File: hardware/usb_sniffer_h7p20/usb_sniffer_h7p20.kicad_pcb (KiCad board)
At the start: 4 copper layers, 45 x 45 mm, 122 parts, among them J2 USB_C_Receptacle_USB2.0_16P, J3 USB_A, J4 USB_C_Receptacle_USB2.0_16P, J5 FFC-40P-0.5mm,NC, U1 H7P20N0L128-M3H1, U11 EA3036C, U2 LM2903, U3 LM2903, U4 LM2903, U5 USB3343, U6 P25Q32SH-SSH-IT, U7 CY7C68013A-56LTX, U8 24C64BN, X1 XO32,26M,NC, Y1 26M,NC, Y2 24M

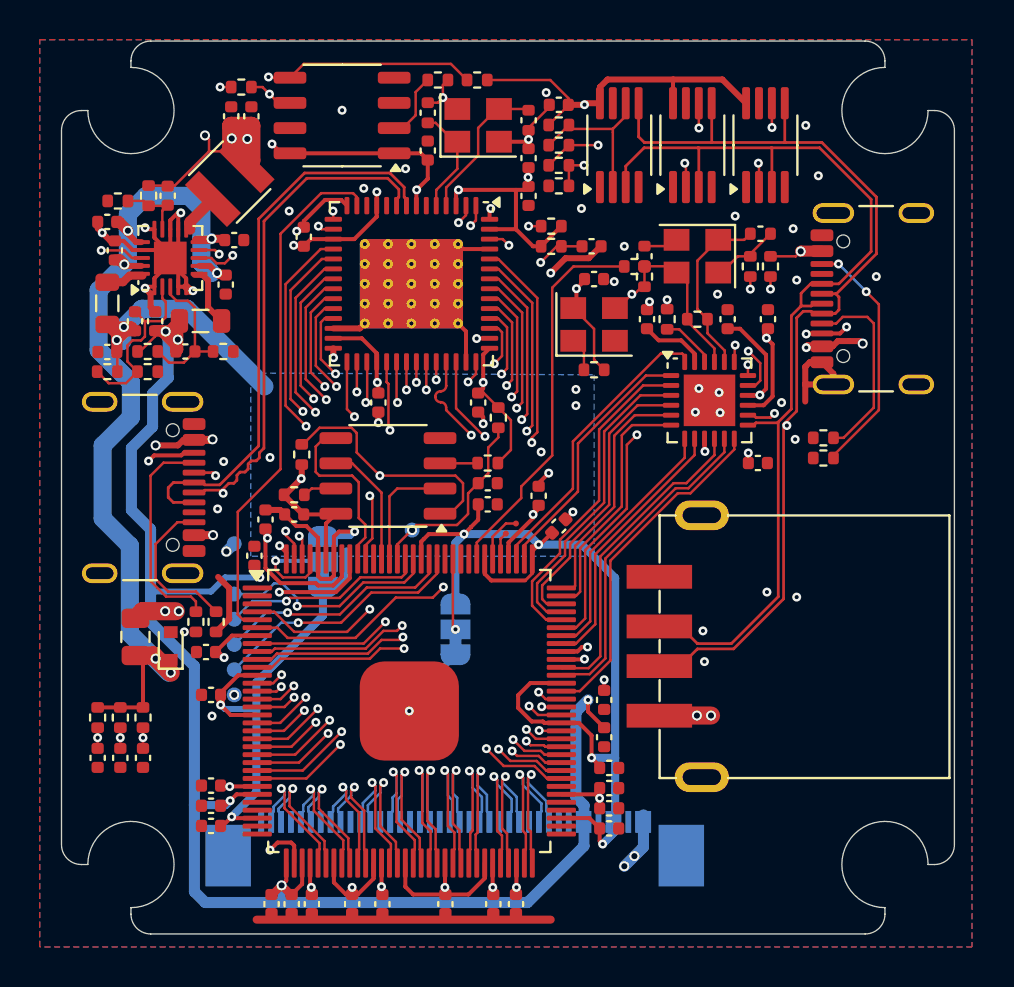
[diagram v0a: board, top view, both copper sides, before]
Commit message: 增加辅助电路和优化焊盘工艺
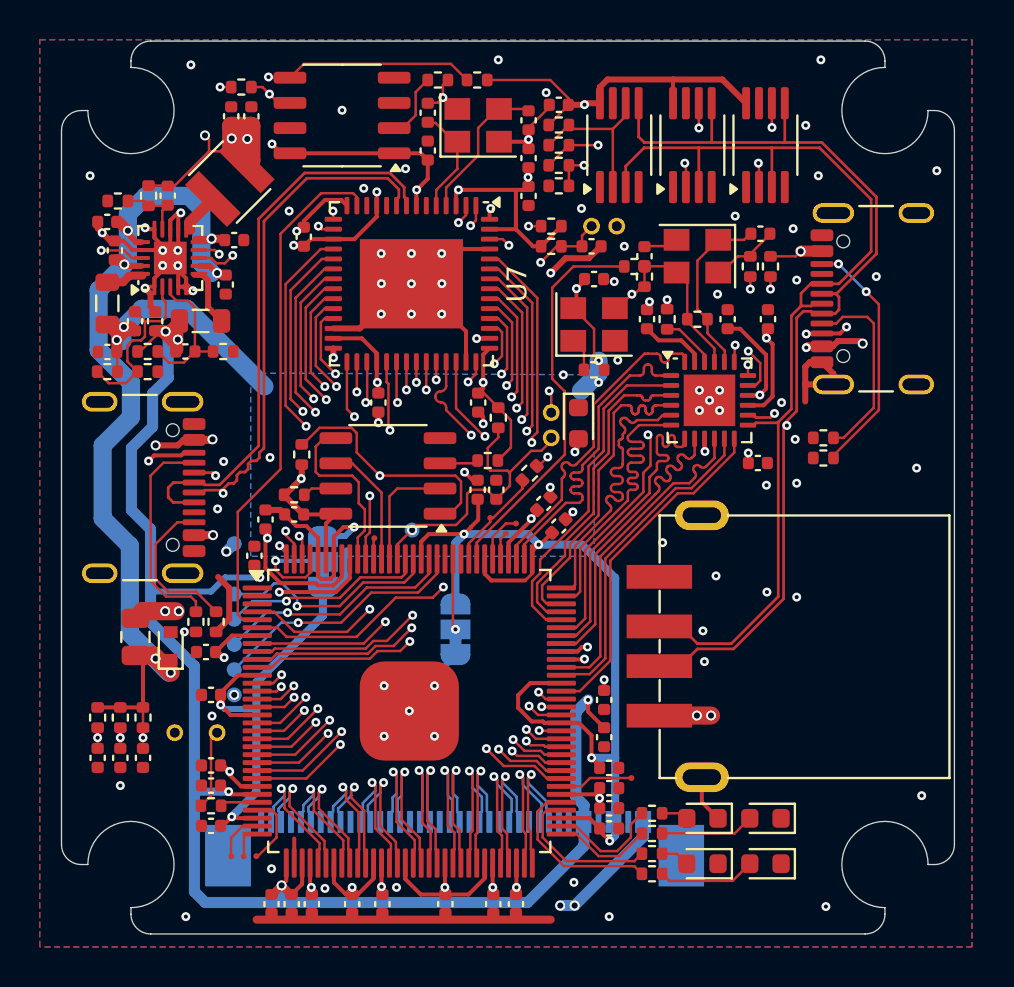
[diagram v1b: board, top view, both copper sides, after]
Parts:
- added D2: LED_RED, LED_SMD:LED_0603_1608Metric, F.Cu at (122.3, 114.2)
- added D3: LED_BLUE, LED_SMD:LED_0603_1608Metric, F.Cu at (125.5, 114.2)
- added D4: LED_YELLOW, LED_SMD:LED_0603_1608Metric, F.Cu at (122.3, 116.5)
- added D5: LED_GREEN, LED_SMD:LED_0603_1608Metric, F.Cu at (125.5, 116.5)
- added D6: LED_GREEN, LED_SMD:LED_0603_1608Metric, F.Cu at (116.1, 94.3)
- added R10: 4.7k, Resistor_SMD:R_0402_1005Metric, F.Cu at (119.8, 116.0)
- added R11: 5.1k, Resistor_SMD:R_0402_1005Metric, F.Cu at (119.8, 117.0)
- added R12: 5.1k, Resistor_SMD:R_0402_1005Metric, F.Cu at (113.6, 96.8)
- added R7: 470, Resistor_SMD:R_0402_1005Metric, F.Cu at (97.5, 113.5)
- added R8: 10k, Resistor_SMD:R_0402_1005Metric, F.Cu at (119.8, 113.9)
- added R9: 5.1k, Resistor_SMD:R_0402_1005Metric, F.Cu at (119.8, 114.9)
- added TP1: TestPoint, vllogic:PinHeader_1x01_P1.00mm_Vertical, F.Cu at (114.7, 95.0)
- added TP14: TestPoint, vllogic:PinHeader_1x01_P1.00mm_Vertical, F.Cu at (97.8, 109.9)
- added TP15: TestPoint, vllogic:PinHeader_1x01_P1.00mm_Vertical, F.Cu at (95.7, 109.9)
- added TP18: TestPoint, vllogic:TestPoint_Pad_D0.3mm, F.Cu at (111.6, 99.0)
- added TP19: TestPoint, vllogic:TestPoint_Pad_D0.3mm, F.Cu at (105.8, 100.1)
- added TP2: TestPoint, vllogic:PinHeader_1x01_P1.00mm_Vertical, F.Cu at (114.7, 93.7)
- added TP20: TestPoint, vllogic:TestPoint_Pad_D0.3mm, F.Cu at (99.8, 116.1)
- added TP21: TestPoint, vllogic:TestPoint_Pad_D0.3mm, F.Cu at (98.6, 116.1)
- added TP22: TestPoint, vllogic:TestPoint_Pad_D0.3mm, F.Cu at (99.2, 116.1)
- added TP23: TestPoint, vllogic:TestPoint_Pad_D0.3mm, F.Cu at (118.7, 112.1)
- added TP3: TestPoint, vllogic:PinHeader_1x01_P1.00mm_Vertical, F.Cu at (118.0, 84.3)
- added TP4: TestPoint, vllogic:PinHeader_1x01_P1.00mm_Vertical, F.Cu at (116.7, 84.3)
- C27: value 4.7uF -> 10uF
- C31, C32: value 20pF -> 12pF; footprint vllogic:C_0402_6mil -> Capacitor_SMD:C_0402_1005Metric
- C38: value 1uF -> NC
- C40: value 1uF,NC -> 1uF
- C5, C7: value 20pF,NC -> NC; footprint vllogic:C_0402_6mil -> Capacitor_SMD:C_0402_1005Metric
- L2, L3: value 1.5uH -> 4.7uH,MPL2012S4R7MHT
- R15, R16, R17: value 2.2k -> 4.7k
- R27: value 1M,NC -> NC
- R29: value 33,NC -> NC
- R30: value 8.06k -> 8.06k,1%
- R37: value 0 -> NC
- U7: footprint Package_DFN_QFN:QFN-56-1EP_8x8mm_P0.5mm_EP4.5x5.2mm_ThermalVias_TopTented -> Package_DFN_QFN:QFN-56-1EP_8x8mm_P0.5mm_EP4.5x5.2mm
- moved C52 1.02 mm to (97.5, 111.5)
- moved C50 1.02 mm to (97.5, 112.5)
- moved C18 0.89 mm to (111.0, 97.6), turned to -90 degrees
- moved C2 0.54 mm to (111.9, 97.6), turned to -90 degrees
- moved C46 0.46 mm to (114.3, 98.3), turned to -135 degrees
- moved R6 0.13 mm to (111.5, 96.1)
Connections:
- C38 pad 2: /ET3036C/EA3036_EN2 -> /VCC_5V
- J4 pad A8: unconnected-(J4-SBU1-PadA8) -> GND
- R37 pad 1: /ET3036C/EA3036_EN2 -> /VCC_5V
- U1 pad 105: unconnected-(U1-IO26_CDONE_2-Pad105) -> /FPGA_CDONE
- U1 pad 117: unconnected-(U1-IO16_GCLK_1-Pad117) -> Net-(U1-IO16_GCLK_1)
- U1 pad 28: unconnected-(U1-IO17_7-Pad28) -> /B7_IO_28
- U1 pad 29: unconnected-(U1-IO18_7-Pad29) -> Net-(U1-IO18_7)
- U1 pad 31: unconnected-(U1-IO21_7-Pad31) -> Net-(U1-IO21_7)
- U1 pad 32: unconnected-(U1-IO22_7-Pad32) -> Net-(U1-IO22_7)
- U1 pad 65: unconnected-(U1-IO1_4-Pad65) -> /LED_BLUE
- U1 pad 66: unconnected-(U1-IO2_4-Pad66) -> /LED_RED
- U1 pad 68: unconnected-(U1-IO7_4-Pad68) -> /LED_YELLOW
- U1 pad 69: unconnected-(U1-IO8_4-Pad69) -> /LED_GREEN
- U1 pad 71: unconnected-(U1-IO9_4-Pad71) -> Net-(U1-IO9_4)
- U11 pad 8: /ET3036C/EA3036_EN2 -> /VCC_5V
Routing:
- net /VCC_5V: track 94.0 -> 128.8 mm, vias 9 -> 11
- net /ET3036C/EA3036_EN2: track 34.0 -> 0.00 mm, vias 2 -> 0
- net /LED_GREEN: track 0.00 -> 8.78 mm
- net /LED_YELLOW: track 0.00 -> 7.85 mm
- net /CRST_N: track 9.92 -> 15.7 mm
- net /LED_RED: track 0.00 -> 5.76 mm
- net /FPGA_CDONE: track 0.00 -> 5.17 mm
- net /LED_BLUE: track 0.00 -> 5.00 mm
- net Net-(D5-A): track 0.00 -> 4.92 mm
- net Net-(D3-A): track 0.00 -> 4.73 mm
- net Net-(R7-Pad1): track 0.00 -> 4.02 mm
- net /USB334x_D2: track 12.5 -> 16.3 mm
- net Net-(U1-IO9_4): track 0.00 -> 3.70 mm
- net Net-(U1-IO18_7): track 0.00 -> 3.62 mm
- net /USB334x_D3: track 12.9 -> 16.5 mm
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
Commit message: hardware\usb_sniffer_h7p20\production_files.2025605
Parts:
- removed D4: LED_YELLOW, LED_SMD:LED_0603_1608Metric
- removed D5: LED_GREEN, LED_SMD:LED_0603_1608Metric
- removed R10: 4.7k, Resistor_SMD:R_0402_1005Metric
- removed R11: 5.1k, Resistor_SMD:R_0402_1005Metric
- removed TP23, TP5: TestPoint, vllogic:TestPoint_Pad_D0.3mm
- added C19: NC, Capacitor_SMD:C_0402_1005Metric, F.Cu at (117.3, 117.2)
- added C54: NC, Capacitor_SMD:C_0402_1005Metric, F.Cu at (117.3, 118.3)
- added C56: NC, Capacitor_SMD:C_0402_1005Metric, F.Cu at (97.5, 110.5)
- added C58: 0.1uF, Capacitor_SMD:C_0402_1005Metric, F.Cu at (101.4, 118.5)
- added C62: 10uF, Capacitor_SMD:C_0402_1005Metric, F.Cu at (102.5, 118.5)
- added JP3: SolderJumper_2_Open, Jumper:SolderJumper-2_P1.3mm_Open_RoundedPad1.0x1.5mm, B.Cu at (103.7, 102.8)
- added JP4: SolderJumper_2_Open, Jumper:SolderJumper-2_P1.3mm_Open_RoundedPad1.0x1.5mm, B.Cu at (103.7, 105.0)
- added R24: 10k,1%, Resistor_SMD:R_0402_1005Metric, F.Cu at (97.7, 115.5)
- added TP16: TestPoint, vllogic:TestPoint_Pad_D0.3mm, F.Cu at (99.2, 102.0)
- added U9: CJ3439KDW, Package_TO_SOT_SMD:SOT-363_SC-70-6, F.Cu at (99.3, 117.4)
- C2: value 0.1uF -> 1uF
- JP2: value SolderJumper_3_Bridged12 -> SolderJumper_2_Open; footprint Jumper:SolderJumper-3_P1.3mm_Bridged12_RoundedPad1.0x1.5mm_NumberLabels -> Jumper:SolderJumper-2_P1.3mm_Open_RoundedPad1.0x1.5mm
- R12, R13, R18, R2, R25, R26, R3, R36, R4, R9: value 5.1k -> 5.1k,1%
- R19, R20, R28, R31, R34, R38, R5, R6, R8: value 10k -> 10k,1%
- R21: value 33k -> 33k,1%
- R32: value 10k -> 150k,1%
- R33, R39: value 10k -> 33k,1%
- R35, R40: value 10k -> 20k,1%
- moved C41 9.14 mm to (110.7, 118.5)
- moved C13 9.14 mm to (109.7, 118.5)
- moved TP14 2.61 mm to (95.6, 111.3), turned to 90 degrees
- moved TP21 1.44 mm to (98.8, 114.7)
- moved C53 1.02 mm to (108.3, 118.5)
- moved C59 0.91 mm to (103.5, 118.5)
- moved JP2 0.81 mm to (103.7, 100.7), turned to 0 degrees
- moved TP15 0.74 mm to (95.6, 109.1), turned to 90 degrees
- moved TP20 0.56 mm to (99.8, 115.5)
- moved TP22 0.56 mm to (99.2, 115.5)
- moved C44 0.51 mm to (105.2, 118.5)
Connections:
- C47 pad 2: /VCCAUX -> /VDDIO_1V8
- C53 pad 2: /VCCAUX -> /VDDIO_1V8
- JP2 pad 1: /VCC_3V3 -> /FPGA_MSEL0
- JP2 pad 2: Net-(JP2-C) -> /VCC_3V3
- U1 pad 1: unconnected-(U1-IO6_8-Pad1) -> Net-(U1-IO6_8)
- U1 pad 102: Net-(U1-IO33_MISO3_2) -> /USB20_DP_CMP2
- U1 pad 106: unconnected-(U1-IO25_GCLK_2-Pad106) -> /USB20_DP_CMP3
- U1 pad 108: unconnected-(U1-IO24_GCLK_1-Pad108) -> /USB20_DM_CMP3
- U1 pad 122: GND -> /FPGA_MSEL0
- U1 pad 124: GND -> /FPGA_MSEL1
- U1 pad 125: Net-(JP2-C) -> /FPGA_MSEL2
- U1 pad 33: /VCCAUX -> /VDDIO_1V8
- U1 pad 35: /VCCAUX -> /VDDIO_1V8
- U1 pad 39: /VCCAUX -> /VDDIO_1V8
- U1 pad 48: /VCCAUX -> /VDDIO_1V8
- U1 pad 53: /VCCAUX -> /VDDIO_1V8
- U1 pad 62: /VCCAUX -> /VDDIO_1V8
- U1 pad 68: /LED_YELLOW -> /USB20_DM_CMP1
- U1 pad 69: /LED_GREEN -> /USB20_DM_CMP2
- U1 pad 71: Net-(U1-IO9_4) -> /USB20_DP_CMP1
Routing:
- net /USB20_DM_CMP2: track 0.00 -> 62.8 mm, vias 0 -> 2
- net /USB20_DM_CMP1: track 0.00 -> 57.0 mm, vias 0 -> 2
- net /USB20_DP_CMP1: track 0.00 -> 49.0 mm, vias 0 -> 2
- net /USB20_DM_CMP3: track 0.00 -> 29.9 mm, vias 0 -> 2
- net /USB20_DP_CMP3: track 0.00 -> 26.2 mm, vias 0 -> 2
- net /VDDIO_1V8: track 0.00 -> 26.0 mm, vias 0 -> 4
- net /USB20_DP_CMP2: track 0.00 -> 23.3 mm, vias 0 -> 2
- net /VCCAUX: track 109.5 -> 97.7 mm, vias 11 -> 10
- net GND: track 95.2 -> 85.2 mm, vias 93 -> 94
- net /LED_GREEN: track 8.78 -> 0.00 mm
- net /FPGA_MSEL2: track 0.00 -> 7.89 mm, vias 0 -> 1
- net /LED_YELLOW: track 7.85 -> 0.00 mm
- net Net-(JP2-C): track 5.56 -> 0.00 mm, vias 1 -> 0
- net /FPGA_MSEL1: track 0.00 -> 5.47 mm, vias 0 -> 1
- net /VDD_CORE: track 120.9 -> 126.1 mm, vias 13 -> 14
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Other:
- board text added: "USB Sniffer H7P20 20250605"

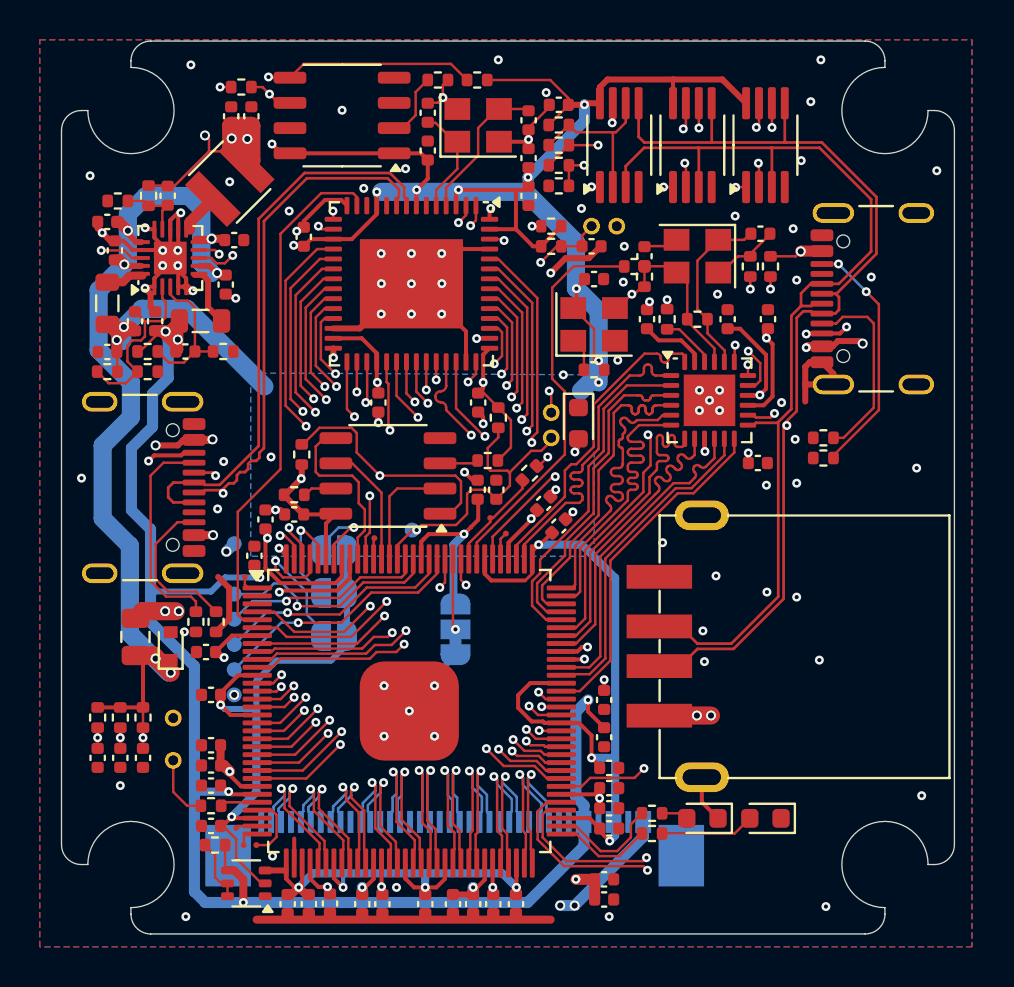
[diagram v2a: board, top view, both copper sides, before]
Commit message: 调整上电顺序为 5V -> core 0.95V -> vccaux 1.8V -> vccio
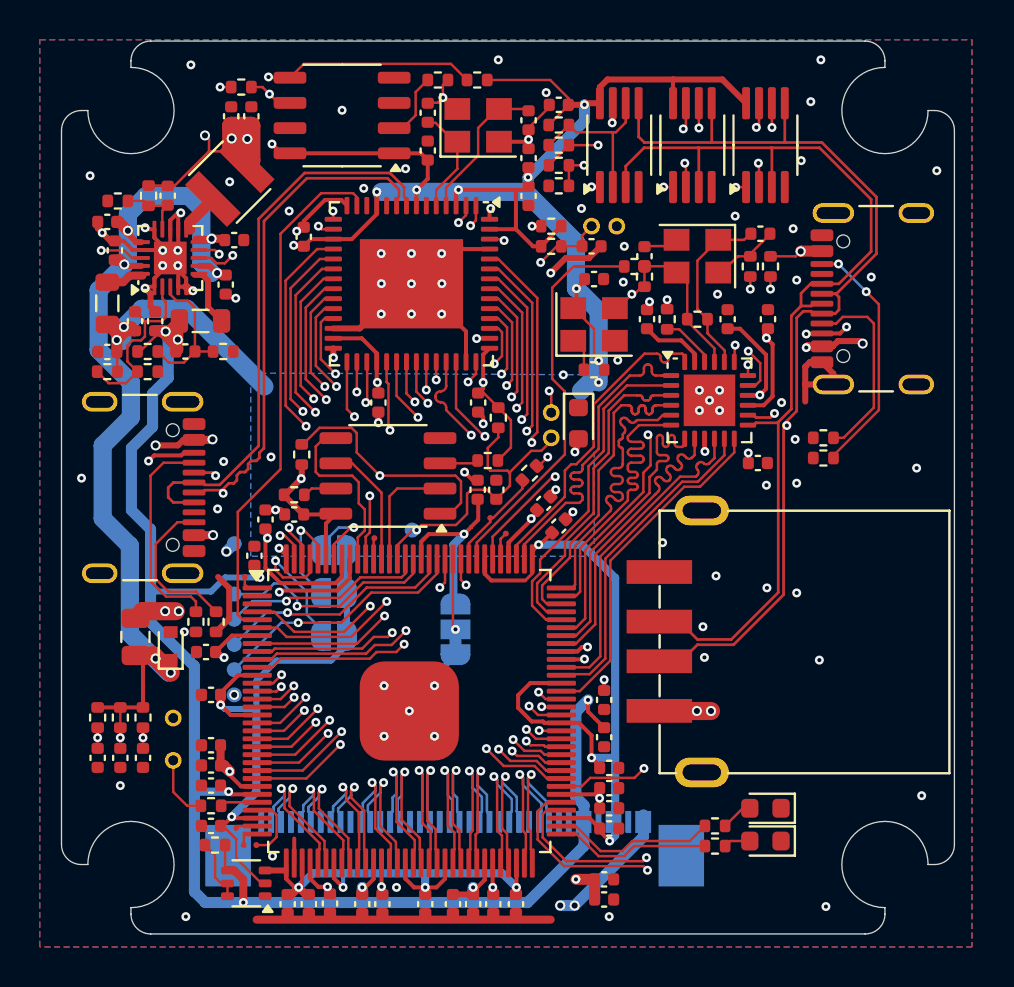
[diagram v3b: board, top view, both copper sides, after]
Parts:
- C38: value NC -> 1uF
- C40: value 1uF -> NC
- R36: value 5.1k,1% -> NC
- R37: value NC -> 10k,1%
- R38: value 10k,1% -> 20k,1%
- moved R8 3.24 mm to (122.9, 114.6)
- moved R9 3.24 mm to (122.9, 115.6)
- moved D2 3.22 mm to (125.5, 113.7)
- moved D3 1.14 mm to (125.5, 115.3)
- moved J3 0.24 mm to (120.1, 105.3)
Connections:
- C38 pad 2: /VCC_5V -> /ET3036C/EA3036_EN2
- C40 pad 2: /ET3036C/EA3036_EN1 -> /VCC_5V
- R36 pad 1: /ET3036C/EA3036_EN1 -> /VCC_5V
- R37 pad 1: /VCC_5V -> /ET3036C/EA3036_EN2
- U11 pad 8: /VCC_5V -> /ET3036C/EA3036_EN2
- U11 pad 9: /ET3036C/EA3036_EN1 -> /VCC_5V
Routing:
- net /ET3036C/EA3036_EN2: track 0.00 -> 34.0 mm, vias 0 -> 2
- net /ET3036C/EA3036_EN1: track 33.0 -> 0.00 mm, vias 2 -> 0
- net Net-(D3-A): track 4.73 -> 1.35 mm
- net /LED_BLUE: track 5.00 -> 7.91 mm
- net /LED_RED: track 5.76 -> 8.28 mm
- net GND: track 85.2 -> 82.8 mm
- net /VCC_5V: track 128.8 -> 127.8 mm

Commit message: 更新丝印
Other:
- board text added: "USB Sniffer H7P20 20250606"
- board text removed: "USB Sniffer H7P20 20250605"
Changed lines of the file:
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@@
   (gr_arc (start 134 78.5) (mid 134.707107 78.792893) (end 135 79.5)
     (stroke (width 0.05) (type solid)) (layer "Edge.Cuts"))
-  (gr_text "USB Sniffer H7P20\n20250605" (at 119.1006 106.8324) (layer "B.SilkS")
+  (gr_text "USB Sniffer H7P20\n20250606" (at 119.1006 106.8324) (layer "B.SilkS")
     (effects (font (size 1 1) (thickness 0.15)) (justify right bottom mirror))
   )
